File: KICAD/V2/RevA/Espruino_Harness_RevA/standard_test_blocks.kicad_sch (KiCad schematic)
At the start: 98 parts, among them J201 EXTERNAL_ANALOG_STIMULUS_0_TO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, J301 GROVE_I2C, J302 MCP23017_GPIO, J401 MCP3008_ANALOGUE_BREAKOUT, J402 ADAFRUIT_MICROSD_BFF_5683, J501 DS18B20_SENSOR_A, J502 DS18B20_SENSOR_B, J503 2K2_DQ_4K7, J504 DS2413_MODULE, J701 UART_PEER, J702 UART_B_DIAGNOSTIC_NO_DRIVE, J902 PIXEL_SHIFTER_6066, Q301 2N7002, Q302 2N7002, U301 MCP23017-E/SO, U401 MCP3008, U701 TMUX1511

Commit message: Verify TB09 addressable RGB baseline
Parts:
- J902: MPN (none) -> 61300411021; now not fitted
- R901: AISLER_MPN (none) -> 470R 0603 1% 0.1W
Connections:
- net TEST_BLOCK_3V3: now also J902.2 (Pin_2); no longer J902.1 (Pin_1)
- net TI_GND: now also J902.1 (Pin_1); no longer J902.2 (Pin_2)
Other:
- note added: "Adafruit Pixel Shifter - Output Logic D5 - 5V level shifted data line output to addressable RGB LED. !D5 - Inverted 5V level shifted data line output to addressable RGB LED. C5 - 5V level shifted clock line output to your addressable RGB LED."
- note added: "Adafruit Pixel Shifter 6066"
- note added: "FUNCTIONAL FLOW"
- note added: "Integration of Removable Adafruit Pixel Shifter 6066; protected 3.3 V data observation"
- note added: "Route and verify TI_RGB_DATA before enabling the target output. Start with the target output low or high impedance. Fit or remove the module only with Test Block power off and the route open. J902 supplies 3.3 V only; module-generated 5 V remains module-local. TP901 is for high-impedance observation only. J902 and TP901/TP902 are DNP / hand-fit parts."
- note added: "Target output → TI_RGB_DATA → R901 470R → RGB_DATA_PROTECTED → TP901 / J902 DAT → Adafruit 6066 level shifter → onboard NeoPixel TEST_BLOCK_3V3 → J902 pin 2 V C901 100nF bypasses TEST_BLOCK_3V3 to TI_GND TI_GND → J902 pin 1 G / TP902; J902 pin 4 CLK is NC"
- note removed: "Pin 1 V; pin 2 GND; pin 3 DAT; pin 4 CLK / NC"
- note removed: "Removable Adafruit Pixel Shifter 6066; protected 3.3 V data observation"
- moved on the sheet: C301, C701, J301, J302, J701, J702, JP301, JP302, JP303, JP306, JP307, JP308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

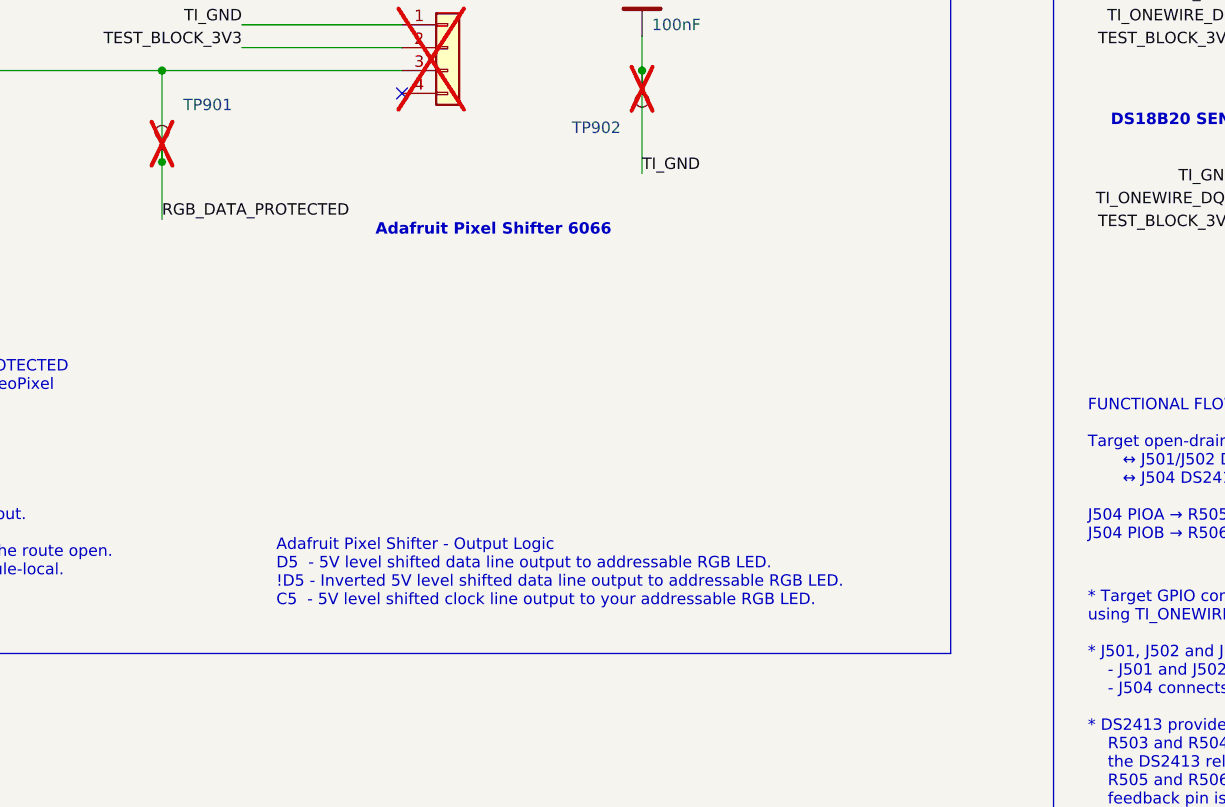
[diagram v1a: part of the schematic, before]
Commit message: Verify TI01 target interface baseline
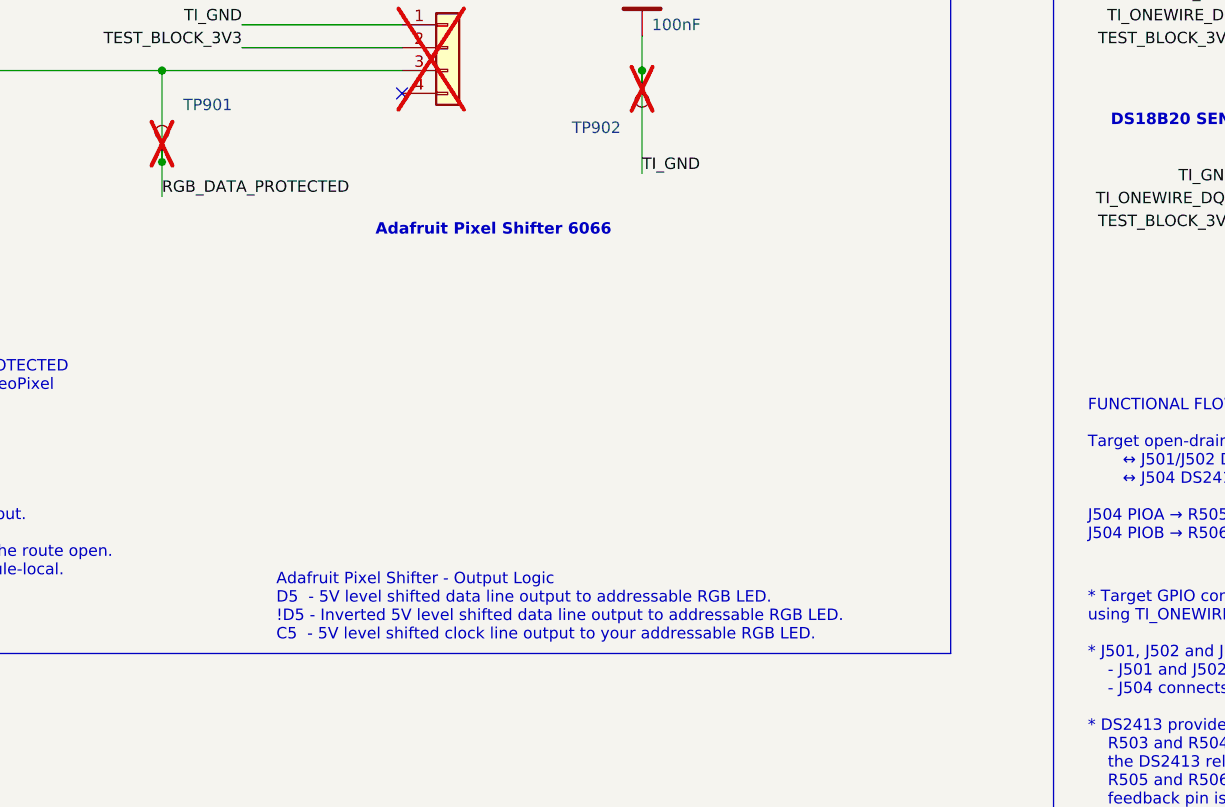
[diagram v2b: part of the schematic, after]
